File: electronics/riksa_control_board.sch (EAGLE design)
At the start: 75 parts

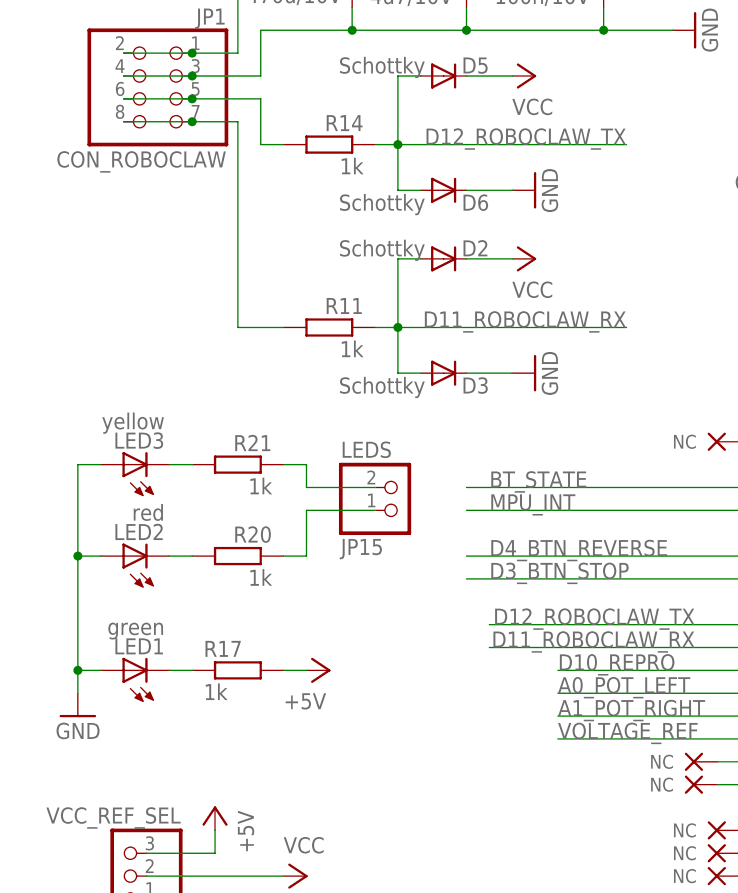
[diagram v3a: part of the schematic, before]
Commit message: ELE: some improves in layout and schema by @PetrBobcik
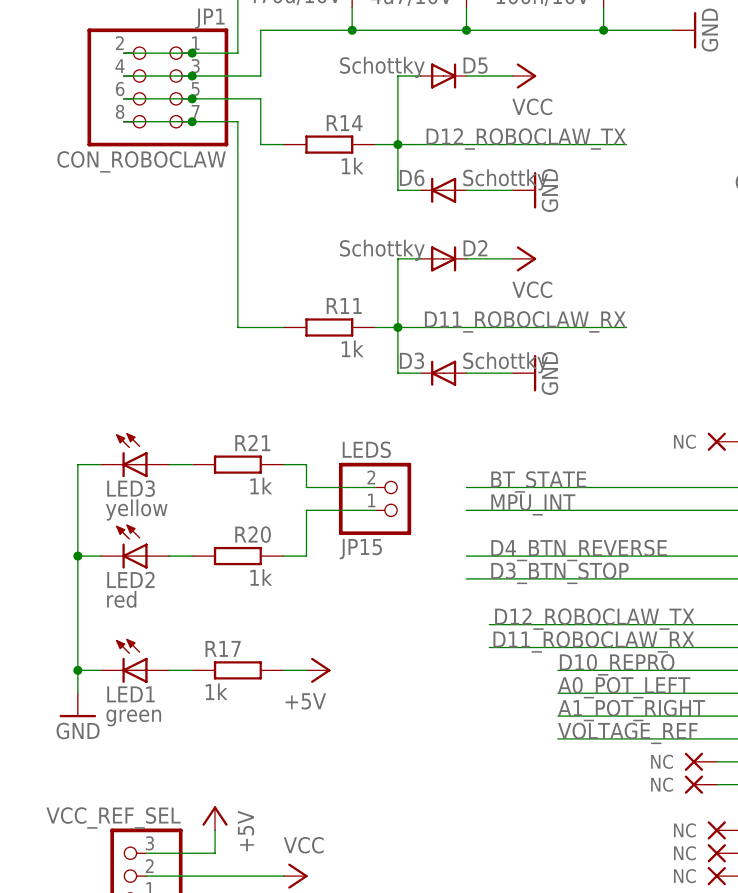
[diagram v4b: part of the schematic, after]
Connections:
- removed net LED_GREEN_: LED1.C, R17.1
- removed net LED_RED_: LED2.C, R20.2
- removed net LED_YELLOW_: LED3.C, R21.2
- new net N$11: LED1.A, R17.1
- new net N$2: LED3.A, R21.2
- new net N$8: LED2.A, R20.2
- net D11_ROBOCLAW_RX: now also D3.C; no longer D3.A
- net D12_ROBOCLAW_TX: now also D6.C; no longer D6.A
- net GND: now also D3.A, D6.A, LED1.C, LED2.C, LED3.C; no longer D3.C, D6.C, LED1.A, LED2.A, LED3.A
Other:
- moved on the sheet: D3, D6, LED1, LED2, LED3
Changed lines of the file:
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@@
 <attribute name="VALUE" x="107.95" y="17.018" size="1.778" layer="96"/>
 </instance>
-<instance part="LED1" gate="G$1" x="15.24" y="86.36" rot="R90"/>
+<instance part="LED1" gate="G$1" x="17.78" y="86.36" rot="R270"/>
 <instance part="GND3" gate="1" x="10.16" y="81.28" rot="MR0"/>
 <instance part="P+7" gate="1" x="25.4" y="71.12" rot="MR0"/>
@@
 <attribute name="VALUE" x="48.768" y="134.1374" size="1.778" layer="96" rot="R180"/>
 </instance>
-<instance part="D3" gate="1" x="50.8" y="119.38" smashed="yes">
-<attribute name="OC_FARNELL" x="50.8" y="119.38" size="2.54" layer="96" display="off"/>
-<attribute name="NAME" x="55.88" y="118.8974" size="1.778" layer="95" rot="R180"/>
-<attribute name="VALUE" x="48.768" y="118.8974" size="1.778" layer="96" rot="R180"/>
+<instance part="D3" gate="1" x="50.8" y="119.38" smashed="yes" rot="R180">
+<attribute name="OC_FARNELL" x="50.8" y="119.38" size="2.54" layer="96" rot="R180" display="off"/>
+<attribute name="NAME" x="45.72" y="119.8626" size="1.778" layer="95"/>
+<attribute name="VALUE" x="52.832" y="119.8626" size="1.778" layer="96"/>
 </instance>
 <instance part="P+12" gate="VCC" x="60.96" y="152.4" rot="MR90"/>
@@
 <attribute name="VALUE" x="48.768" y="154.4574" size="1.778" layer="96" rot="R180"/>
 </instance>
-<instance part="D6" gate="1" x="50.8" y="139.7" smashed="yes">
-<attribute name="OC_FARNELL" x="50.8" y="139.7" size="2.54" layer="96" display="off"/>
-<attribute name="NAME" x="55.88" y="139.2174" size="1.778" layer="95" rot="R180"/>
-<attribute name="VALUE" x="48.768" y="139.2174" size="1.778" layer="96" rot="R180"/>
+<instance part="D6" gate="1" x="50.8" y="139.7" smashed="yes" rot="R180">
+<attribute name="OC_FARNELL" x="50.8" y="139.7" size="2.54" layer="96" rot="R180" display="off"/>
+<attribute name="NAME" x="45.72" y="140.1826" size="1.778" layer="95"/>
+<attribute name="VALUE" x="52.832" y="140.1826" size="1.778" layer="96"/>
 </instance>
 <instance part="R15" gate="G$1" x="139.7" y="147.32" smashed="yes" rot="R90">
@@
 <attribute name="VALUE" x="31.75" y="105.918" size="1.778" layer="96" rot="MR0"/>
 </instance>
-<instance part="LED2" gate="G$1" x="15.24" y="99.06" rot="R90"/>
-<instance part="LED3" gate="G$1" x="15.24" y="109.22" rot="R90"/>
+<instance part="LED2" gate="G$1" x="17.78" y="99.06" rot="R270"/>
+<instance part="LED3" gate="G$1" x="17.78" y="109.22" rot="R270"/>
 </instances>
 <busses>
@@
 <wire x1="71.12" y1="124.46" x2="45.72" y2="124.46" width="0.1524" layer="91"/>
 <wire x1="45.72" y1="124.46" x2="43.18" y2="124.46" width="0.1524" layer="91"/>
-<wire x1="45.72" y1="119.38" x2="48.26" y2="119.38" width="0.1524" layer="91"/>
 <wire x1="45.72" y1="124.46" x2="45.72" y2="119.38" width="0.1524" layer="91"/>
 <junction x="45.72" y="124.46"/>
@@
 <label x="71.12" y="124.46" size="1.778" layer="95" rot="MR0"/>
 <pinref part="D2" gate="1" pin="A"/>
-<pinref part="D3" gate="1" pin="A"/>
+<pinref part="D3" gate="1" pin="C"/>
+<wire x1="48.26" y1="119.38" x2="45.72" y2="119.38" width="0.1524" layer="91"/>
 </segment>
 <segment>
@@
 <wire x1="71.12" y1="144.78" x2="45.72" y2="144.78" width="0.1524" layer="91"/>
 <wire x1="45.72" y1="144.78" x2="43.18" y2="144.78" width="0.1524" layer="91"/>
-<wire x1="45.72" y1="139.7" x2="48.26" y2="139.7" width="0.1524" layer="91"/>
 <wire x1="45.72" y1="144.78" x2="45.72" y2="139.7" width="0.1524" layer="91"/>
 <junction x="45.72" y="144.78"/>
@@
 <label x="71.12" y="144.78" size="1.778" layer="95" rot="MR0"/>
 <pinref part="D5" gate="1" pin="A"/>
-<pinref part="D6" gate="1" pin="A"/>
+<pinref part="D6" gate="1" pin="C"/>
+<wire x1="45.72" y1="139.7" x2="48.26" y2="139.7" width="0.1524" layer="91"/>
 </segment>
 </net>
@@
 </segment>
 <segment>
+<pinref part="GND3" gate="1" pin="GND"/>
+<wire x1="10.16" y1="83.82" x2="10.16" y2="86.36" width="0.1524" layer="91"/>
+<pinref part="LED3" gate="G$1" pin="C"/>
+<wire x1="10.16" y1="86.36" x2="10.16" y2="99.06" width="0.1524" layer="91"/>
+<wire x1="10.16" y1="99.06" x2="10.16" y2="109.22" width="0.1524" layer="91"/>
+<wire x1="10.16" y1="109.22" x2="12.7" y2="109.22" width="0.1524" layer="91"/>
+<pinref part="LED2" gate="G$1" pin="C"/>
+<wire x1="12.7" y1="99.06" x2="10.16" y2="99.06" width="0.1524" layer="91"/>
+<junction x="10.16" y="99.06"/>
+<pinref part="LED1" gate="G$1" pin="C"/>
+<wire x1="12.7" y1="86.36" x2="10.16" y2="86.36" width="0.1524" layer="91"/>
+<junction x="10.16" y="86.36"/>
+</segment>
+<segment>
+<pinref part="D6" gate="1" pin="A"/>
+<pinref part="GND13" gate="1" pin="GND"/>
+<wire x1="53.34" y1="139.7" x2="58.42" y2="139.7" width="0.1524" layer="91"/>
+</segment>
+<segment>
+<pinref part="D3" gate="1" pin="A"/>
 <pinref part="GND12" gate="1" pin="GND"/>
-<wire x1="58.42" y1="119.38" x2="53.34" y2="119.38" width="0.1524" layer="91"/>
-<pinref part="D3" gate="1" pin="C"/>
-</segment>
-<segment>
-<pinref part="LED1" gate="G$1" pin="A"/>
-<wire x1="12.7" y1="86.36" x2="10.16" y2="86.36" width="0.1524" layer="91"/>
-<wire x1="10.16" y1="86.36" x2="10.16" y2="83.82" width="0.1524" layer="91"/>
-<pinref part="GND3" gate="1" pin="GND"/>
-<wire x1="10.16" y1="86.36" x2="10.16" y2="99.06" width="0.1524" layer="91"/>
-<junction x="10.16" y="86.36"/>
-<pinref part="LED2" gate="G$1" pin="A"/>
-<wire x1="10.16" y1="99.06" x2="12.7" y2="99.06" width="0.1524" layer="91"/>
-<wire x1="10.16" y1="99.06" x2="10.16" y2="109.22" width="0.1524" layer="91"/>
-<junction x="10.16" y="99.06"/>
-<pinref part="LED3" gate="G$1" pin="A"/>
-<wire x1="10.16" y1="109.22" x2="12.7" y2="109.22" width="0.1524" layer="91"/>
-</segment>
-<segment>
-<pinref part="GND13" gate="1" pin="GND"/>
-<wire x1="58.42" y1="139.7" x2="53.34" y2="139.7" width="0.1524" layer="91"/>
-<pinref part="D6" gate="1" pin="C"/>
+<wire x1="53.34" y1="119.38" x2="58.42" y2="119.38" width="0.1524" layer="91"/>
 </segment>
 </net>
@@
 </segment>
 </net>
-<net name="LED_GREEN_" class="0">
-<segment>
-<pinref part="LED1" gate="G$1" pin="C"/>
-<pinref part="R17" gate="G$1" pin="1"/>
-<wire x1="22.86" y1="86.36" x2="20.32" y2="86.36" width="0.1524" layer="91"/>
-</segment>
-</net>
-<net name="LED_YELLOW_" class="0">
-<segment>
-<pinref part="LED3" gate="G$1" pin="C"/>
-<pinref part="R21" gate="G$1" pin="2"/>
-<wire x1="20.32" y1="109.22" x2="22.86" y2="109.22" width="0.1524" layer="91"/>
-</segment>
-</net>
-<net name="LED_RED_" class="0">
-<segment>
-<pinref part="LED2" gate="G$1" pin="C"/>
-<pinref part="R20" gate="G$1" pin="2"/>
-<wire x1="20.32" y1="99.06" x2="22.86" y2="99.06" width="0.1524" layer="91"/>
-</segment>
-</net>
 <net name="LED_RED" class="0">
 <segment>
@@
 </segment>
 </net>
+<net name="N$2" class="0">
+<segment>
+<pinref part="R21" gate="G$1" pin="2"/>
+<pinref part="LED3" gate="G$1" pin="A"/>
+<wire x1="22.86" y1="109.22" x2="20.32" y2="109.22" width="0.1524" layer="91"/>
+</segment>
+</net>
+<net name="N$8" class="0">
+<segment>
+<pinref part="LED2" gate="G$1" pin="A"/>
+<pinref part="R20" gate="G$1" pin="2"/>
+<wire x1="20.32" y1="99.06" x2="22.86" y2="99.06" width="0.1524" layer="91"/>
+</segment>
+</net>
+<net name="N$11" class="0">
+<segment>
+<pinref part="LED1" gate="G$1" pin="A"/>
+<pinref part="R17" gate="G$1" pin="1"/>
+<wire x1="20.32" y1="86.36" x2="22.86" y2="86.36" width="0.1524" layer="91"/>
+</segment>
+</net>

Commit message: ELE: final version of board
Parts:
- added C5: 470u/10V, rcl:CPOL-EUTT6D6
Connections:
- net +5V: now also C5.+
- net GND: now also C5.-
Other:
- note added: "Released under the Creative Commons Attribution-ShareAlike 4.0 License https://creativecommons.org/licenses/by-sa/4.0/ Designed by: JM & JP & JS & JV & RobotikaBrno RB3200-ESP32universal https://github.com/RoboticsBrno/RB3200-ESP32universal RobotikaBrno.cz Robotarna"
- note added: "RobotikaBrno"
- note added: "github:roboticsbrno/ RB3200-ESP32universal RobotikaBrno.cz Robotarna CC BY-SA 4.0"
- note added: "v2.1"
- moved on the sheet: C2, C3
